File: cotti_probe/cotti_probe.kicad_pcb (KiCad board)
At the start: 4 copper layers, 61 x 88.9 mm, 114 parts, among them J1 Conn_01x02, J2 Conn_01x02, J3 Pmod UART 2x06 pin, J4 Pmod UART 2x06 pin, J5 Pmod GPIO 2x06 pin, J6 Pmod SPI 2x06 pin, J7 USB_C (16 + 8), Q1 RE1C001ZPTL, U1 FT4232HL, U2 TLV74333PDBVR, U3 93LC46BT-I/OT, U4 74HC595D, Y1 XTAL 12MHz 20pF

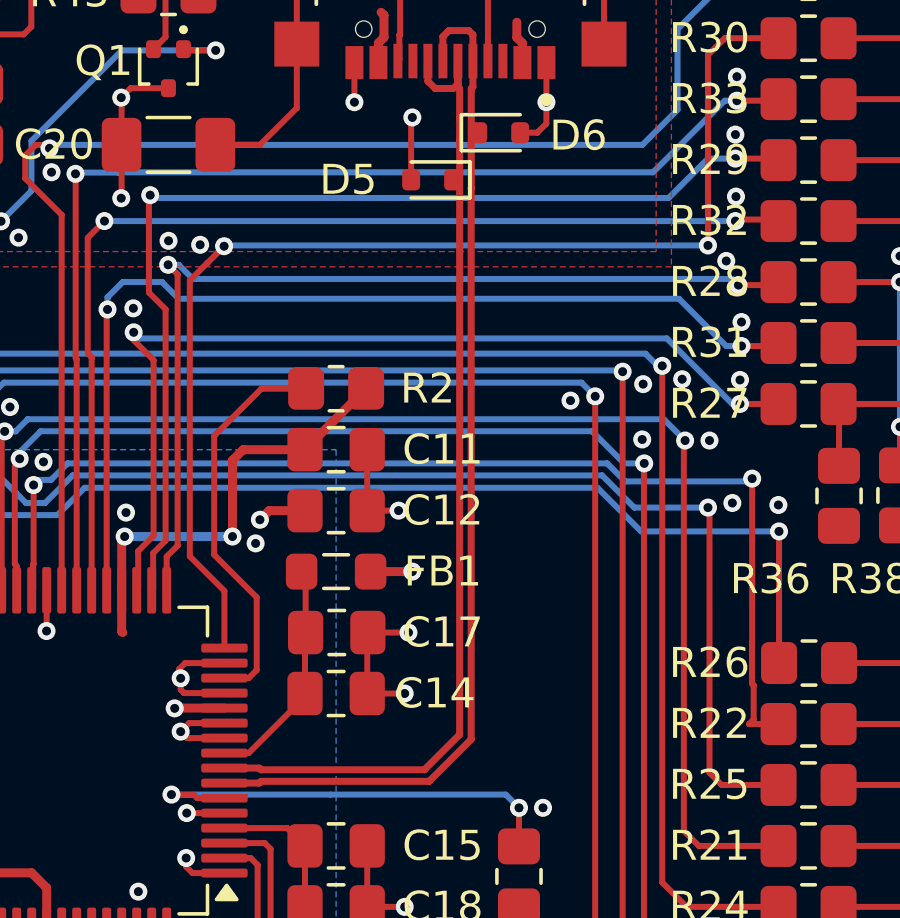
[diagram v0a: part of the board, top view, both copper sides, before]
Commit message: fix: length tune usb in probe
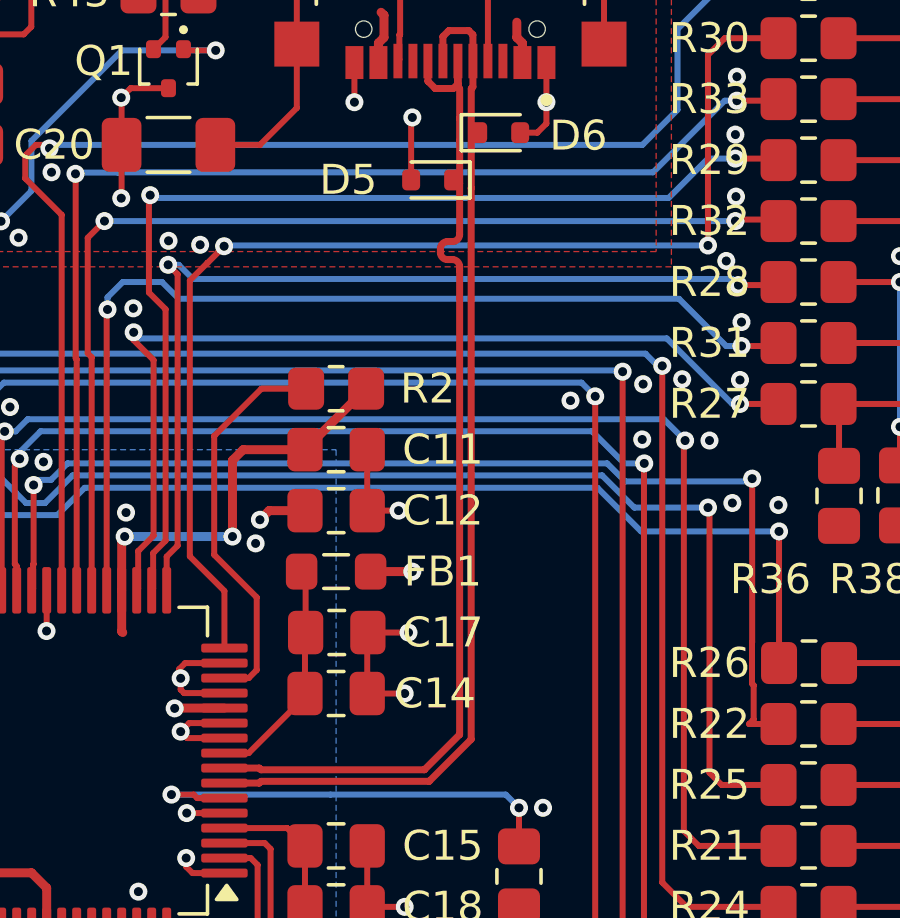
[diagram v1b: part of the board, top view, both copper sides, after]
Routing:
- net /D+: track 33.4 -> 34.3 mm
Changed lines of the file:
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@@
 	)
 	(segment
-		(start 164.13815 35.430436)
-		(end 164.13815 36.846688)
+		(start 163.08 33.4384)
+		(end 163.322 33.6804)
 		(width 0.2337)
 		(layer "F.Cu")
@@
 	)
 	(segment
-		(start 163.08 33.4384)
-		(end 163.322 33.6804)
+		(start 164.13815 33.686651)
+		(end 164.13815 34.673564)
 		(width 0.2337)
 		(layer "F.Cu")
@@
 	)
 	(segment
-		(start 164.08 33.628501)
-		(end 164.13815 33.686651)
+		(start 163.89715 38.783311)
+		(end 163.735279 38.783311)
 		(width 0.2337)
 		(layer "F.Cu")
@@
 	)
 	(segment
-		(start 164.13715 55.215838)
-		(end 162.962638 56.39035)
+		(start 163.735279 39.383311)
+		(end 163.89715 39.383311)
 		(width 0.2337)
 		(layer "F.Cu")
@@
 	)
 	(segment
-		(start 163.08 32.766)
-		(end 163.08 33.4384)
+		(start 164.13695 35.429236)
+		(end 164.13815 35.430436)
+		(width 0.2337)
+		(layer "F.Cu")
+		(net 61)
+	)
+	(segment
+		(start 157.459501 56.3332)
+		(end 156.297 56.3332)
+		(width 0.2337)
+		(layer "F.Cu")
+		(net 61)
+	)
+	(segment
+		(start 164.08 32.766)
+		(end 164.08 33.628501)
+		(width 0.2337)
+		(layer "F.Cu")
+		(net 61)
+	)
+	(segment
+		(start 164.13815 36.846688)
+		(end 164.13715 36.847688)
+		(width 0.2337)
+		(layer "F.Cu")
+		(net 61)
+	)
+	(segment
+		(start 164.08 33.628501)
+		(end 164.13815 33.686651)
 		(width 0.2337)
 		(layer "F.Cu")
@@
 	)
 	(segment
+		(start 164.13815 35.430436)
+		(end 164.13815 36.846688)
+		(width 0.2337)
+		(layer "F.Cu")
+		(net 61)
+	)
+	(segment
 		(start 164.13815 34.673564)
 		(end 164.13695 34.674764)
@@
 	)
 	(segment
-		(start 163.9276 33.6804)
-		(end 164.08 33.528)
+		(start 163.08 32.766)
+		(end 163.08 33.4384)
 		(width 0.2337)
 		(layer "F.Cu")
@@
 	)
 	(segment
-		(start 164.13815 33.686651)
-		(end 164.13815 34.673564)
+		(start 163.9276 33.6804)
+		(end 164.08 33.528)
 		(width 0.2337)
 		(layer "F.Cu")
@@
 	)
 	(segment
-		(start 164.13715 36.847688)
+		(start 164.13715 40.663282)
 		(end 164.13715 55.215838)
 		(width 0.2337)
@@
 	)
 	(segment
-		(start 164.13815 36.846688)
-		(end 164.13715 36.847688)
+		(start 164.13715 39.623311)
+		(end 164.13715 39.743311)
 		(width 0.2337)
 		(layer "F.Cu")
@@
 	)
 	(segment
-		(start 164.08 33.528)
-		(end 164.08 32.766)
+		(start 157.516651 56.39035)
+		(end 157.459501 56.3332)
 		(width 0.2337)
 		(layer "F.Cu")
@@
 	)
 	(segment
-		(start 164.13695 35.429236)
-		(end 164.13815 35.430436)
+		(start 164.13715 55.215838)
+		(end 162.962638 56.39035)
 		(width 0.2337)
 		(layer "F.Cu")
@@
 	)
 	(segment
-		(start 157.459501 56.3332)
-		(end 156.297 56.3332)
+		(start 163.495279 39.023311)
+		(end 163.495279 39.143311)
 		(width 0.2337)
 		(layer "F.Cu")
@@
 	)
 	(segment
-		(start 163.322 33.6804)
-		(end 163.9276 33.6804)
+		(start 164.13715 39.743311)
+		(end 164.13715 40.663282)
 		(width 0.2337)
 		(layer "F.Cu")
@@
 	)
 	(segment
-		(start 157.516651 56.39035)
-		(end 157.459501 56.3332)
+		(start 164.08 33.528)
+		(end 164.08 32.766)
 		(width 0.2337)
 		(layer "F.Cu")
@@
 	)
 	(segment
-		(start 164.08 32.766)
-		(end 164.08 33.628501)
+		(start 164.13715 36.847688)
+		(end 164.13715 38.543311)
+		(width 0.2337)
+		(layer "F.Cu")
+		(net 61)
+	)
+	(segment
+		(start 163.322 33.6804)
+		(end 163.9276 33.6804)
+		(width 0.2337)
+		(layer "F.Cu")
+		(net 61)
+	)
+	(arc
+		(start 163.89715 39.383311)
+		(mid 164.066856 39.453605)
+		(end 164.13715 39.623311)
+		(width 0.2337)
+		(layer "F.Cu")
+		(net 61)
+	)
+	(arc
+		(start 163.495279 39.143311)
+		(mid 163.565573 39.313017)
+		(end 163.735279 39.383311)
+		(width 0.2337)
+		(layer "F.Cu")
+		(net 61)
+	)
+	(arc
+		(start 164.13715 38.543311)
+		(mid 164.066856 38.713017)
+		(end 163.89715 38.783311)
+		(width 0.2337)
+		(layer "F.Cu")
+		(net 61)
+	)
+	(arc
+		(start 163.735279 38.783311)
+		(mid 163.565573 38.853605)
+		(end 163.495279 39.023311)
 		(width 0.2337)
 		(layer "F.Cu")
@@
 			(pts
 				(xy 165.608 33.528) (xy 165.4556 57.912) (xy 154.94 57.912) (xy 154.94 55.372) (xy 162.052 55.372)
-				(xy 163.068 54.356) (xy 163.2204 33.528)
+				(xy 163.068 54.356) (xy 163.195 40.513) (xy 162.052 40.513) (xy 162.052 37.846) (xy 163.195 37.846)
+				(xy 163.2204 33.528)
 			)
 		)
@@
 		)
 	)
+	(generated
+		(type tuning_pattern)
+		(name "Tuning Pattern")
+		(layer "F.Cu")
+		(base_line
+			(pts
+				(xy 164.13715 38.543311) (xy 164.13715 40.663282)
+			)
+		)
+		(base_line_coupled
+			(pts
+				(xy 164.52185 38.543311) (xy 164.52185 38.571023)
+			)
+		)
+		(corner_radius_percent 80)
+		(end
+			(xy 164.13715 40.663282)
+		)
+		(initial_side "right")
+		(last_diff_pair_gap 0.18)
+		(last_netname "/D+")
+		(last_status "tuned")
+		(last_track_width 0.2337)
+		(last_tuning "-0.0000 in (tuned)")
+		(max_amplitude 1)
+		(min_amplitude 0.2)
+		(min_spacing 0.6)
+		(origin
+			(xy 164.13715 38.543311)
+		)
+		(override_custom_rules no)
+		(rounded yes)
+		(single_sided no)
+		(target_length 1000000)
+		(target_length_max 1000000)
+		(target_length_min 0)
+		(target_skew 0)
+		(target_skew_max 0.1)
+		(target_skew_min -0.1)
+		(tuning_mode "diff_pair_skew")
+		(members "2517eabb-8097-435a-8662-b2c3b0379ca0" "32537e99-cdd3-49c7-9508-b348fdf77311"
+			"4ceb455d-d26b-4a52-aa85-80aee9f6eb11" "8a9e6d27-7411-4b2e-91b3-bc0ef0bd63b8"
+			"988db9c4-9398-4988-ab78-92ce97b4b7e1" "99db9bf6-14bc-4b2f-adec-0c329de58884"
+			"bc20cb9f-ad52-45dc-8d26-e0c078048ff6" "bc966012-0172-422d-a849-a3b81d21de74"
+			"c358a5d1-f9b5-4f77-8bec-e79c00776c3f"
+		)
+	)
